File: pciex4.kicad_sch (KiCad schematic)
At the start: 17 parts, among them J2 Bus_PCI_Express_x4

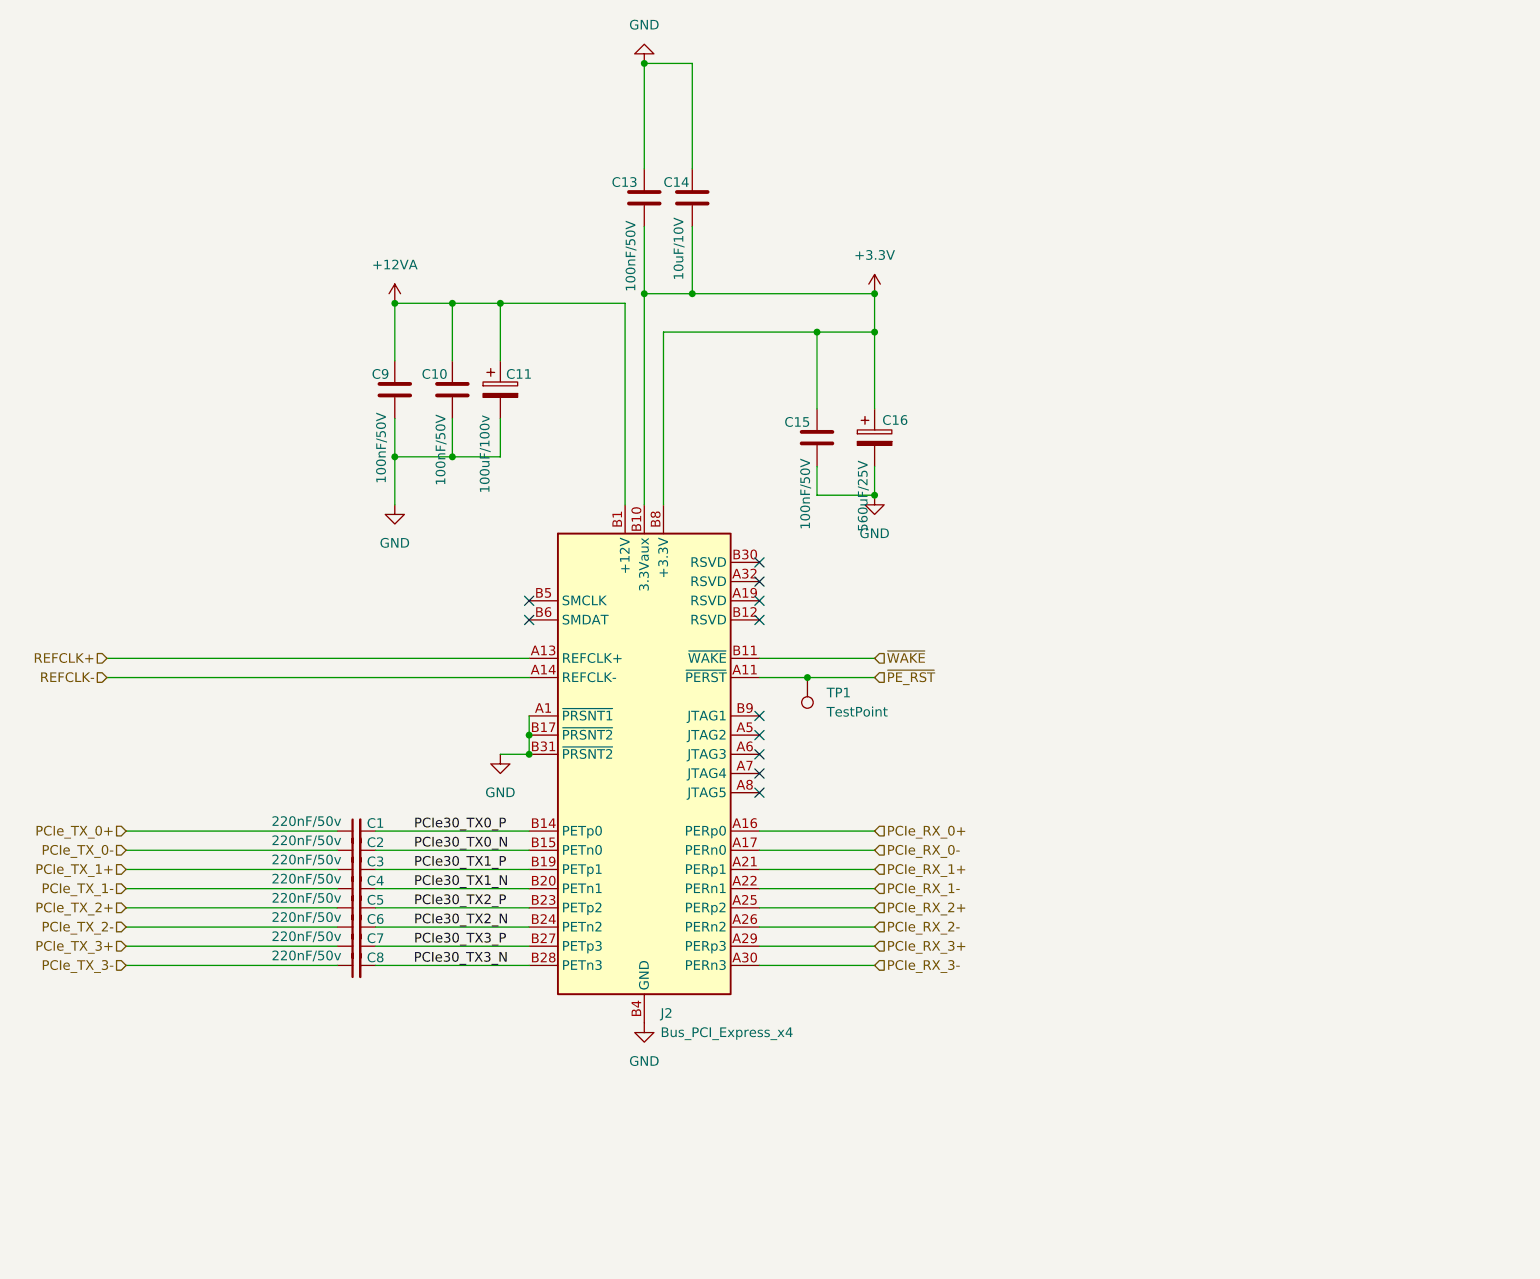
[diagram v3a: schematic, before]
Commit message: Updated all the footprints into the pcb editor but all the designator numbers have changed... I have tp go back and fix each one
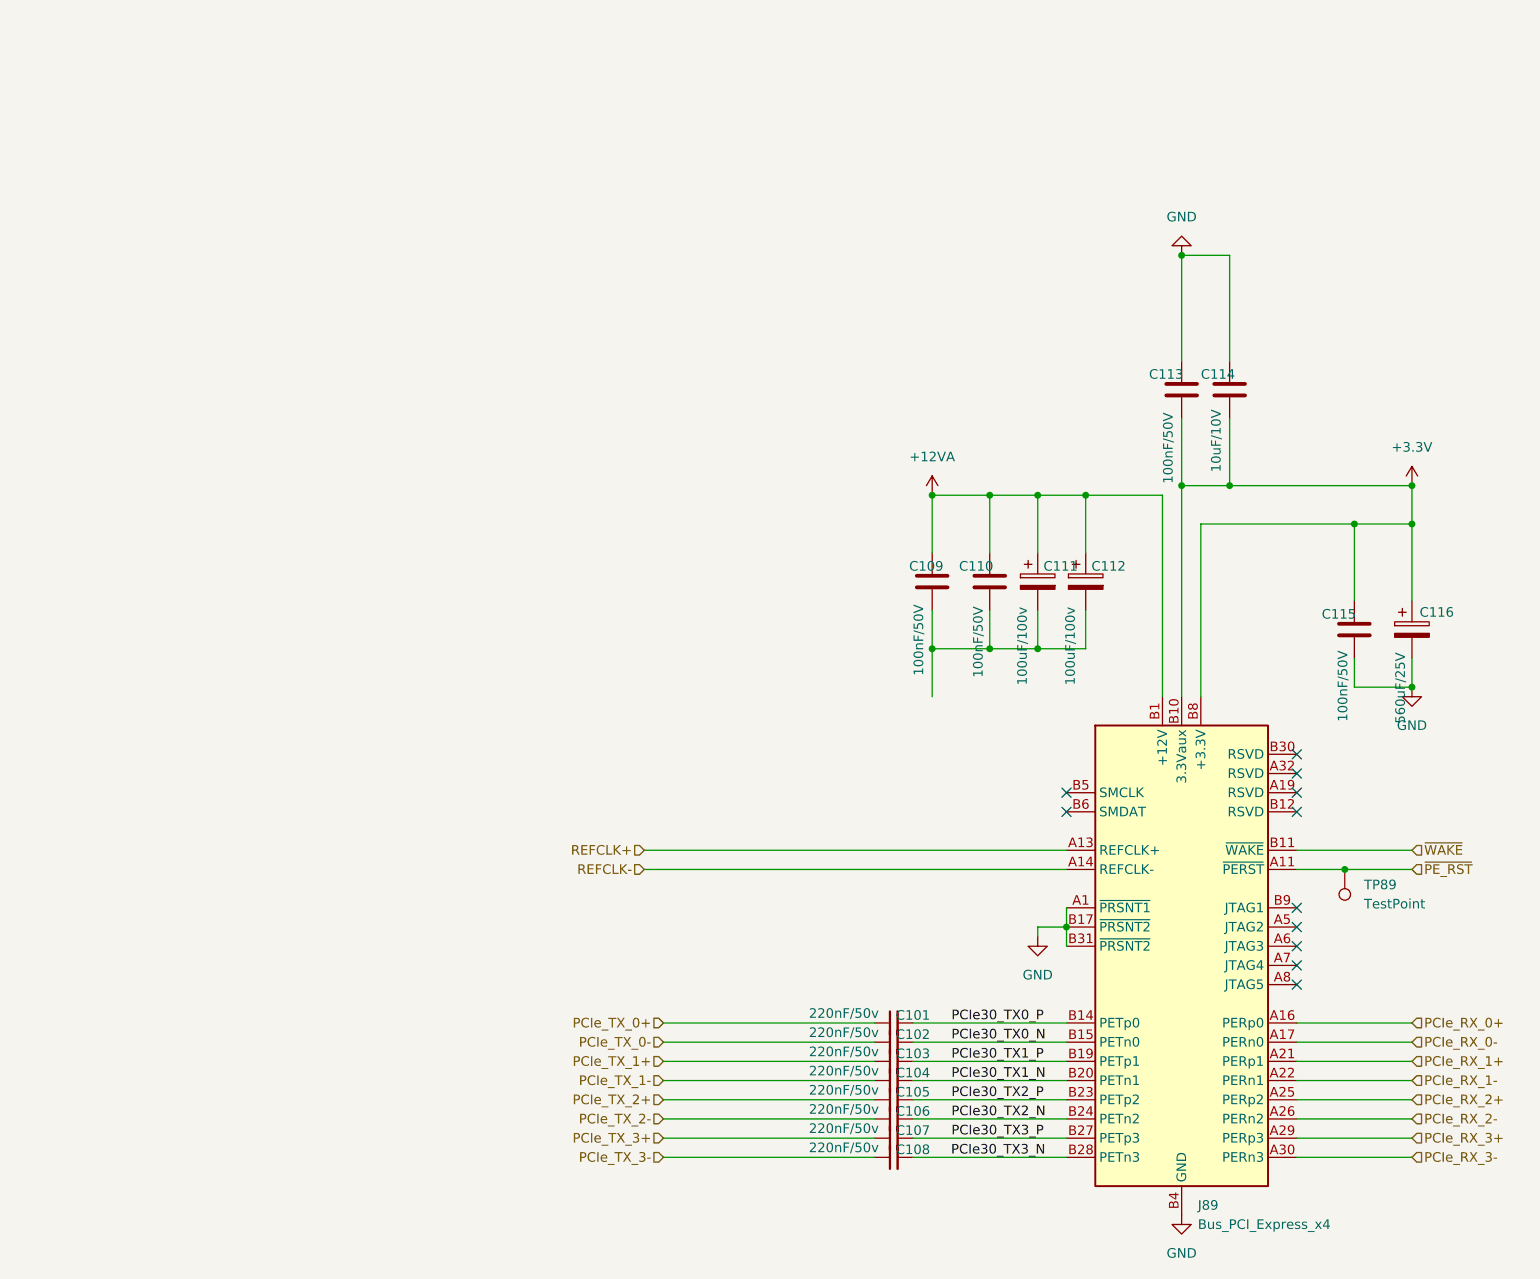
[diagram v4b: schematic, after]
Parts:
- removed C1, C2, C3, C4, C5, C6, C7, C8: 220nF/50v, A_HDJ_Library:C_0402_1005Metric, symbol Device:C_Small
- removed C10, C13, C15, C9: 100nF/50V, A_HDJ_Library:C_0402_1005Metric, symbol Device:C
- removed C11: 100uF/100v, A_HDJ_Library:CP_Elec_6.3x7.7, symbol Device:C_Polarized
- removed C14: 10uF/10V, A_HDJ_Library:C_0402_1005Metric, symbol Device:C
- removed C16: 560uF/25V, A_HDJ_Library:CP_Elec_6.3x7.7, symbol Device:C_Polarized
- removed J2: Bus_PCI_Express_x4, A_HDJ_Library:PCIe_x4_Gen3Slot_Connectors, symbol Connector:Bus_PCI_Express_x4
- removed TP1: TestPoint, symbol Connector:TestPoint
- added C101, C102, C103, C104, C105, C106, C107, C108: 220nF/50v, A_HDJ_Library:C_0402_1005Metric, symbol Device:C_Small
- added C109, C110, C113, C115: 100nF/50V, A_HDJ_Library:C_0402_1005Metric, symbol Device:C
- added C111, C112: 100uF/100v, A_HDJ_Library:CP_Elec_6.3x7.7, symbol Device:C_Polarized
- added C114: 10uF/10V, A_HDJ_Library:C_0402_1005Metric, symbol Device:C
- added C116: 560uF/25V, A_HDJ_Library:CP_Elec_6.3x7.7, symbol Device:C_Polarized
- added J89: Bus_PCI_Express_x4, A_HDJ_Library:PCIe_x4_Gen3Slot_Connectors, symbol Connector:Bus_PCI_Express_x4
- added TP89: TestPoint, A_HDJ_Library:TestPoint_Pad_D1.5mm, symbol Connector:TestPoint
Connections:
- net +12VA: now also C109.1, C110.1, C111.1, C112.1, J89.A2 (+12V), J89.A3 (+12V), J89.B1 (+12V), J89.B2 (+12V), J89.B3 (+12V)
- net +3.3V: now also C113.2, C114.2, C115.1, C116.1, J89.A10 (+3.3V), J89.A9 (+3.3V), J89.B10 (3.3Vaux), J89.B8 (+3.3V)
- net GND: now also C113.1, C114.1, C115.2, C116.2, J89.A1 (~{PRSNT1}), J89.A12 (GND), J89.A15 (GND), J89.A18 (GND), J89.A20 (GND), J89.A23 (GND), J89.A24 (GND), J89.A27 (GND), J89.A28 (GND), J89.A31 (GND), J89.A4 (GND), J89.B13 (GND), J89.B16 (GND), J89.B17 (~{PRSNT2}), J89.B18 (GND), J89.B21 (GND), J89.B22 (GND), J89.B25 (GND), J89.B26 (GND), J89.B29 (GND), J89.B31 (~{PRSNT2}), J89.B32 (GND), J89.B4 (GND), J89.B7 (GND)
- net PCIe30_TX0_N: now also C102.2, J89.B15 (PETn0)
- net PCIe30_TX0_P: now also C101.2, J89.B14 (PETp0)
- net PCIe30_TX1_N: now also C104.2, J89.B20 (PETn1)
- net PCIe30_TX1_P: now also C103.2, J89.B19 (PETp1)
- net PCIe30_TX2_N: now also C106.2, J89.B24 (PETn2)
- net PCIe30_TX2_P: now also C105.2, J89.B23 (PETp2)
- net PCIe30_TX3_N: now also C108.2, J89.B28 (PETn3)
- net PCIe30_TX3_P: now also C107.2, J89.B27 (PETp3)
- net PCIe_RX_0+: now also J89.A16 (PERp0)
- net PCIe_RX_0-: now also J89.A17 (PERn0)
- net PCIe_RX_1+: now also J89.A21 (PERp1)
- net PCIe_RX_1-: now also J89.A22 (PERn1)
- net PCIe_RX_2+: now also J89.A25 (PERp2)
- net PCIe_RX_2-: now also J89.A26 (PERn2)
- net PCIe_RX_3+: now also J89.A29 (PERp3)
- net PCIe_RX_3-: now also J89.A30 (PERn3)
- net PCIe_TX_0+: now also C101.1
- net PCIe_TX_0-: now also C102.1
- net PCIe_TX_1+: now also C103.1
- net PCIe_TX_1-: now also C104.1
- net PCIe_TX_2+: now also C105.1
- net PCIe_TX_2-: now also C106.1
- net PCIe_TX_3+: now also C107.1
- net PCIe_TX_3-: now also C108.1
- net REFCLK+: now also J89.A13 (REFCLK+)
- net REFCLK-: now also J89.A14 (REFCLK-)
- net ~{PE_RST}: now also J89.A11 (~{PERST}), TP89.1
- net ~{WAKE}: now also J89.B11 (~{WAKE})
- new net: C109.2, C110.2, C111.2, C112.2

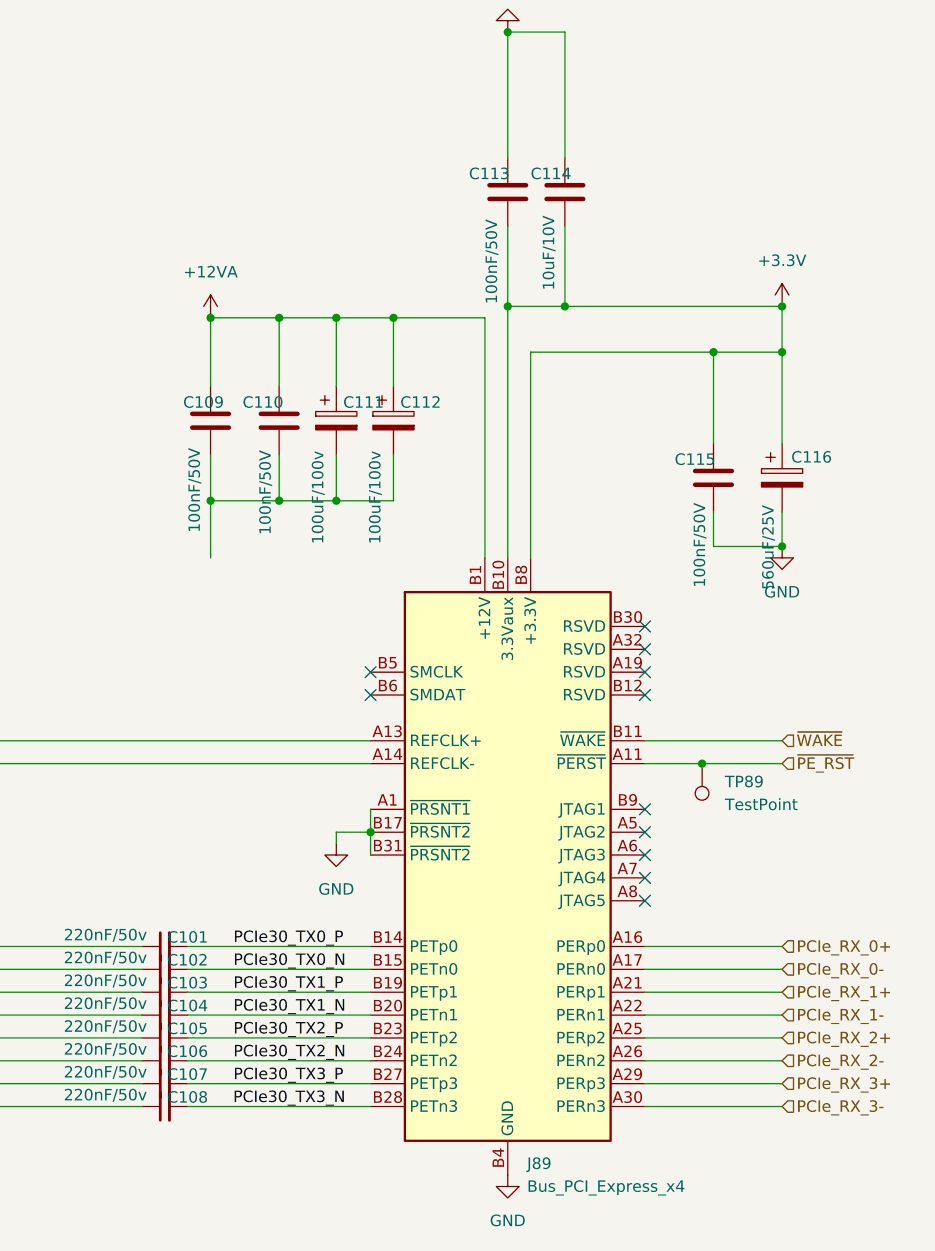
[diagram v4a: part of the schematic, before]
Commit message: Designators in pcie restored
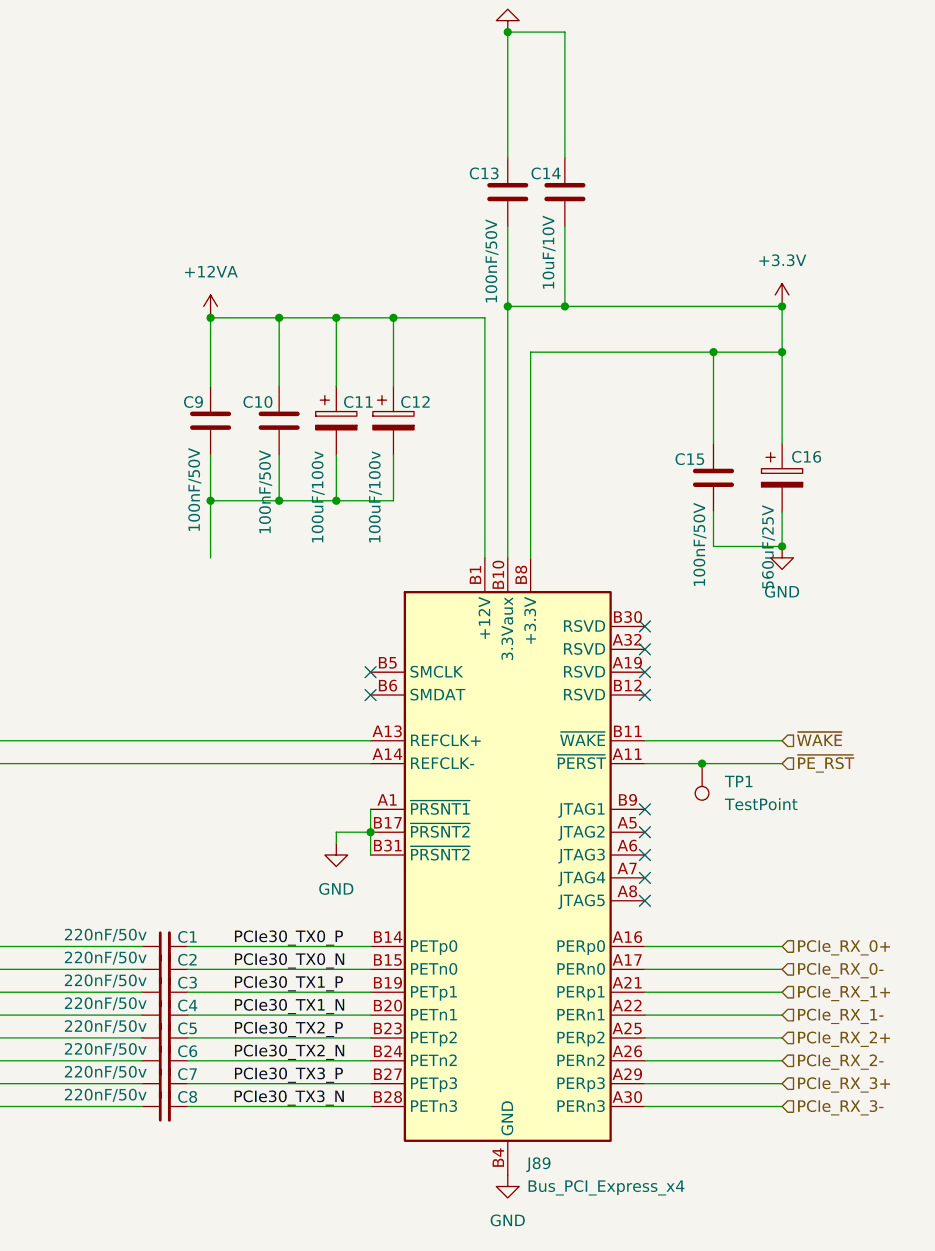
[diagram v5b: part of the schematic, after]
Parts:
- renumbered C101 to C1, C110 to C10, C111 to C11, C112 to C12, C113 to C13, C114 to C14, C115 to C15, C116 to C16, C102 to C2, C103 to C3, C104 to C4, C105 to C5, C106 to C6, C107 to C7, C108 to C8, C109 to C9, TP89 to TP1
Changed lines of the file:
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@@
 		(in_pos_files yes)
 		(dnp no)
-		(property "Reference" "C111"
+		(property "Reference" "C11"
 			(at 192.532 98.298 0)
 			(show_name no)
@@
 			(project "Carrier_Board"
 				(path "/e768274e-12f3-4f83-96f6-abb7638e0bc1/d05d8b94-71f3-437a-a0af-11ed4e3069d0"
-					(reference "C111")
+					(reference "C11")
 					(unit 1)
 				)
@@
 		(in_pos_files yes)
 		(dnp no)
-		(property "Reference" "C106"
+		(property "Reference" "C6"
 			(at 175.26 170.434 90)
 			(show_name no)
@@
 			(project "Carrier_Board"
 				(path "/e768274e-12f3-4f83-96f6-abb7638e0bc1/d05d8b94-71f3-437a-a0af-11ed4e3069d0"
-					(reference "C106")
+					(reference "C6")
 					(unit 1)
 				)
@@
 		(in_pos_files yes)
 		(dnp no)
-		(property "Reference" "C105"
+		(property "Reference" "C5"
 			(at 175.26 167.894 90)
 			(show_name no)
@@
 			(project "Carrier_Board"
 				(path "/e768274e-12f3-4f83-96f6-abb7638e0bc1/d05d8b94-71f3-437a-a0af-11ed4e3069d0"
-					(reference "C105")
+					(reference "C5")
 					(unit 1)
 				)
@@
 		(in_pos_files yes)
 		(dnp no)
-		(property "Reference" "C116"
+		(property "Reference" "C16"
 			(at 242.316 104.394 0)
 			(show_name no)
@@
 			(project "Carrier_Board"
 				(path "/e768274e-12f3-4f83-96f6-abb7638e0bc1/d05d8b94-71f3-437a-a0af-11ed4e3069d0"
-					(reference "C116")
+					(reference "C16")
 					(unit 1)
 				)
@@
 		(in_pos_files yes)
 		(dnp no)
-		(property "Reference" "C108"
+		(property "Reference" "C8"
 			(at 175.26 175.514 90)
 			(show_name no)
@@
 			(project "Carrier_Board"
 				(path "/e768274e-12f3-4f83-96f6-abb7638e0bc1/d05d8b94-71f3-437a-a0af-11ed4e3069d0"
-					(reference "C108")
+					(reference "C8")
 					(unit 1)
 				)
@@
 		(in_pos_files yes)
 		(dnp no)
-		(property "Reference" "C112"
+		(property "Reference" "C12"
 			(at 198.882 98.298 0)
 			(show_name no)
@@
 			(project "Carrier_Board"
 				(path "/e768274e-12f3-4f83-96f6-abb7638e0bc1/d05d8b94-71f3-437a-a0af-11ed4e3069d0"
-					(reference "C112")
+					(reference "C12")
 					(unit 1)
 				)
@@
 		(in_pos_files yes)
 		(dnp no)
-		(property "Reference" "C113"
+		(property "Reference" "C13"
 			(at 206.502 72.898 0)
 			(show_name no)
@@
 			(project "Carrier_Board"
 				(path "/e768274e-12f3-4f83-96f6-abb7638e0bc1/d05d8b94-71f3-437a-a0af-11ed4e3069d0"
-					(reference "C113")
+					(reference "C13")
 					(unit 1)
 				)
@@
 		(in_pos_files yes)
 		(dnp no)
-		(property "Reference" "C107"
+		(property "Reference" "C7"
 			(at 175.26 172.974 90)
 			(show_name no)
@@
 			(project "Carrier_Board"
 				(path "/e768274e-12f3-4f83-96f6-abb7638e0bc1/d05d8b94-71f3-437a-a0af-11ed4e3069d0"
-					(reference "C107")
+					(reference "C7")
 					(unit 1)
 				)
@@
 		(dnp no)
 		(fields_autoplaced yes)
-		(property "Reference" "TP89"
+		(property "Reference" "TP1"
 			(at 234.95 140.4619 0)
 			(show_name no)
@@
 			(project "Carrier_Board"
 				(path "/e768274e-12f3-4f83-96f6-abb7638e0bc1/d05d8b94-71f3-437a-a0af-11ed4e3069d0"
-					(reference "TP89")
+					(reference "TP1")
 					(unit 1)
 				)
@@
 		(in_pos_files yes)
 		(dnp no)
-		(property "Reference" "C101"
+		(property "Reference" "C1"
 			(at 175.26 157.734 90)
 			(show_name no)
@@
 			(project "Carrier_Board"
 				(path "/e768274e-12f3-4f83-96f6-abb7638e0bc1/d05d8b94-71f3-437a-a0af-11ed4e3069d0"
-					(reference "C101")
+					(reference "C1")
 					(unit 1)
 				)
@@
 		(in_pos_files yes)
 		(dnp no)
-		(property "Reference" "C104"
+		(property "Reference" "C4"
 			(at 175.26 165.354 90)
 			(show_name no)
@@
 			(project "Carrier_Board"
 				(path "/e768274e-12f3-4f83-96f6-abb7638e0bc1/d05d8b94-71f3-437a-a0af-11ed4e3069d0"
-					(reference "C104")
+					(reference "C4")
 					(unit 1)
 				)
@@
 		(in_pos_files yes)
 		(dnp no)
-		(property "Reference" "C114"
+		(property "Reference" "C14"
 			(at 213.36 72.898 0)
 			(show_name no)
@@
 			(project "Carrier_Board"
 				(path "/e768274e-12f3-4f83-96f6-abb7638e0bc1/d05d8b94-71f3-437a-a0af-11ed4e3069d0"
-					(reference "C114")
+					(reference "C14")
 					(unit 1)
 				)
@@
 		(in_pos_files yes)
 		(dnp no)
-		(property "Reference" "C109"
+		(property "Reference" "C9"
 			(at 174.752 98.298 0)
 			(show_name no)
@@
 			(project "Carrier_Board"
 				(path "/e768274e-12f3-4f83-96f6-abb7638e0bc1/d05d8b94-71f3-437a-a0af-11ed4e3069d0"
-					(reference "C109")
+					(reference "C9")
 					(unit 1)
 				)
@@
 		(in_pos_files yes)
 		(dnp no)
-		(property "Reference" "C110"
+		(property "Reference" "C10"
 			(at 181.356 98.298 0)
 			(show_name no)
@@
 			(project "Carrier_Board"
 				(path "/e768274e-12f3-4f83-96f6-abb7638e0bc1/d05d8b94-71f3-437a-a0af-11ed4e3069d0"
-					(reference "C110")
+					(reference "C10")
 					(unit 1)
 				)
@@
 		(in_pos_files yes)
 		(dnp no)
-		(property "Reference" "C115"
+		(property "Reference" "C15"
 			(at 229.362 104.648 0)
 			(show_name no)
@@
 			(project "Carrier_Board"
 				(path "/e768274e-12f3-4f83-96f6-abb7638e0bc1/d05d8b94-71f3-437a-a0af-11ed4e3069d0"
-					(reference "C115")
+					(reference "C15")
 					(unit 1)
 				)
@@
 		(in_pos_files yes)
 		(dnp no)
-		(property "Reference" "C102"
+		(property "Reference" "C2"
 			(at 175.26 160.274 90)
 			(show_name no)
@@
 			(project "Carrier_Board"
 				(path "/e768274e-12f3-4f83-96f6-abb7638e0bc1/d05d8b94-71f3-437a-a0af-11ed4e3069d0"
-					(reference "C102")
+					(reference "C2")
 					(unit 1)
 				)
@@
 		(in_pos_files yes)
 		(dnp no)
-		(property "Reference" "C103"
+		(property "Reference" "C3"
 			(at 175.26 162.814 90)
 			(show_name no)
@@
 			(project "Carrier_Board"
 				(path "/e768274e-12f3-4f83-96f6-abb7638e0bc1/d05d8b94-71f3-437a-a0af-11ed4e3069d0"
-					(reference "C103")
+					(reference "C3")
 					(unit 1)
 				)
